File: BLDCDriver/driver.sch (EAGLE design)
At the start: 66 parts, among them Q2 SIZ240DT-T1-GE3, Q3 SIZ240DT-T1-GE3, Q4 SIZ240DT-T1-GE3, U1 QFN50P400X400X100-25NDRV8300D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, U2 AS5048A-HTSP-500, U3 MCP2562-E/SN, U4 SOP80P620X125-8N, X2 JST-XH-06-PIN-LONG-PAD

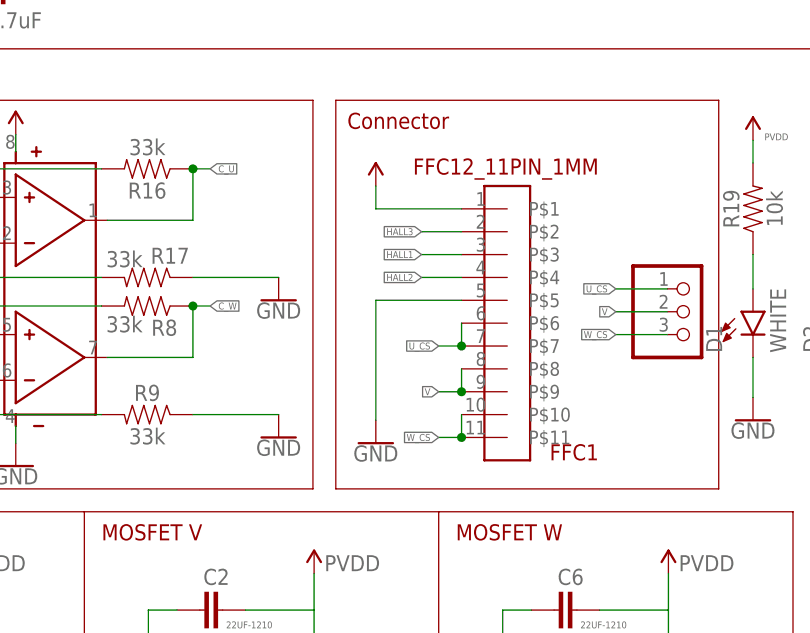
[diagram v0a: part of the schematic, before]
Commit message: ゲートドライバ周りの配線全部終わらせた
# ==== Emojis ====
# ✨ :sparkles: Add new feature
# ✅  :white_check_mark: Update existing feature (not bug)
# ⚠️  :warning: Fix bug/error
# 🔥  :fire: Remove files or features
# ✏️ :pencil2: Fix typos
# 📝  :memo: Update documentation
# ♻️  :recycle: Dependencies update
# 🐧  :penguin: Improved the Linux
# 🍎  :apple: Improved the macOS
# 🔖 :bookmark: Add new library
# 🎉  :tada: Initial commit

# ==== Format ====
# :emoji: Subject
#
# Commit body...

# ==== Messages ====
# 新規(ファイル)機能追加: Add
# 機能修正、既存機能追加（バグではない): Update
# リファクタリング: Clean
# ファイル名変更:
# 削除など: Remove
# バグ修正: Fix
# バージョンアップ: Upgrade
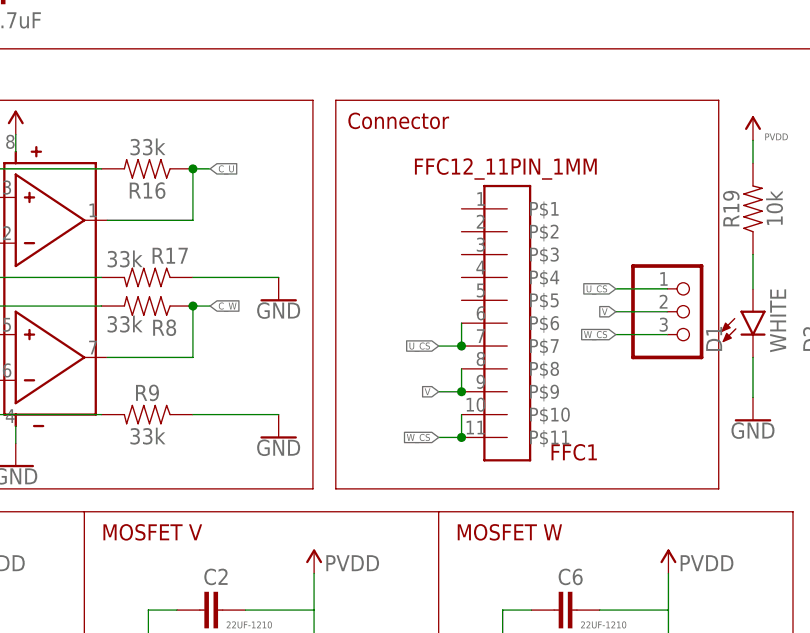
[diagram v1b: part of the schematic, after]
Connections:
- removed net HALL1: FFC1.P$3
- removed net HALL2: FFC1.P$4
- removed net HALL3: FFC1.P$2
- net 5V: no longer FFC1.P$1
- net GND: no longer FFC1.P$5
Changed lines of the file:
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@@
 <part name="GND12" library="SparkFun-PowerSymbols" deviceset="GND" device=""/>
 <part name="FFC1" library="MotorDriver_FourthEdition_prot" deviceset="FFC12_11PIN_1MM" device=""/>
-<part name="SUPPLY8" library="SparkFun-PowerSymbols" deviceset="VCC_1" device="" value="GVDD"/>
-<part name="GND11" library="SparkFun-PowerSymbols" deviceset="GND" device=""/>
 <part name="U2" library="AS5048A-HTSP-500" deviceset="AS5048A-HTSP-500" device=""/>
 <part name="U4" library="NJM2732" deviceset="SOP80P620X125-8N" device=""/>
@@
 <attribute name="VALUE" x="149.225" y="102.87" size="1.778" layer="94" rot="MR0"/>
 </instance>
-<instance part="SUPPLY8" gate="G$2" x="124.46" y="101.6" smashed="yes"/>
-<instance part="GND11" gate="1" x="124.46" y="73.025" smashed="yes">
-<attribute name="VALUE" x="124.46" y="72.771" size="1.778" layer="96" align="top-center"/>
-</instance>
 <instance part="U2" gate="G$1" x="145.415" y="196.85" smashed="yes">
 <attribute name="NAME" x="135.2441" y="212.1063" size="1.27" layer="95"/>
@@
 <wire x1="4.445" y1="34.29" x2="4.445" y2="31.75" width="0.1524" layer="91"/>
 <pinref part="GND12" gate="1" pin="GND"/>
-</segment>
-<segment>
-<pinref part="FFC1" gate="G$1" pin="P$5"/>
-<pinref part="GND11" gate="1" pin="GND"/>
-<wire x1="124.46" y1="75.565" x2="124.46" y2="88.9" width="0.1524" layer="91"/>
-<wire x1="124.46" y1="88.9" x2="133.985" y2="88.9" width="0.1524" layer="91"/>
 </segment>
 <segment>
@@
 </segment>
 </net>
-<net name="HALL3" class="0">
-<segment>
-<pinref part="FFC1" gate="G$1" pin="P$2"/>
-<wire x1="133.985" y1="96.52" x2="129.54" y2="96.52" width="0.1524" layer="91"/>
-<label x="129.54" y="96.52" size="0.762" layer="95" rot="MR0" xref="yes"/>
-</segment>
-</net>
-<net name="HALL1" class="0">
-<segment>
-<pinref part="FFC1" gate="G$1" pin="P$3"/>
-<wire x1="133.985" y1="93.98" x2="129.54" y2="93.98" width="0.1524" layer="91"/>
-<label x="129.54" y="93.98" size="0.762" layer="95" rot="MR0" xref="yes"/>
-</segment>
-</net>
-<net name="HALL2" class="0">
-<segment>
-<pinref part="FFC1" gate="G$1" pin="P$4"/>
-<wire x1="133.985" y1="91.44" x2="129.54" y2="91.44" width="0.1524" layer="91"/>
-<label x="129.54" y="91.44" size="0.762" layer="95" rot="MR0" xref="yes"/>
-</segment>
-</net>
 <net name="5V" class="0">
 <segment>
-<pinref part="SUPPLY8" gate="G$2" pin="VCC_1"/>
-<pinref part="FFC1" gate="G$1" pin="P$1"/>
-<wire x1="133.985" y1="99.06" x2="124.46" y2="99.06" width="0.1524" layer="91"/>
-<wire x1="124.46" y1="101.6" x2="124.46" y2="99.06" width="0.1524" layer="91"/>
-</segment>
-<segment>
 <wire x1="185.42" y1="60.96" x2="182.88" y2="60.96" width="0.1524" layer="91"/>

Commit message: CANの配線をした
# ==== Emojis ====
# ✨ :sparkles: Add new feature
# ✅  :white_check_mark: Update existing feature (not bug)
# ⚠️  :warning: Fix bug/error
# 🔥  :fire: Remove files or features
# ✏️ :pencil2: Fix typos
# 📝  :memo: Update documentation
# ♻️  :recycle: Dependencies update
# 🐧  :penguin: Improved the Linux
# 🍎  :apple: Improved the macOS
# 🔖 :bookmark: Add new library
# 🎉  :tada: Initial commit

# ==== Format ====
# :emoji: Subject
#
# Commit body...

# ==== Messages ====
# 新規(ファイル)機能追加: Add
# 機能修正、既存機能追加（バグではない): Update
# リファクタリング: Clean
# ファイル名変更:
# 削除など: Remove
# バグ修正: Fix
# バージョンアップ: Upgrade
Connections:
- net CANRX: now also NUCLEO_MAIN.PB9
- net CANTX: now also NUCLEO_MAIN.PB8
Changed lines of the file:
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@@
 <label x="180.34" y="22.86" size="0.762" layer="95" rot="R180" xref="yes"/>
+</segment>
+<segment>
+<pinref part="NUCLEO_MAIN" gate="G$1" pin="PB8"/>
+<wire x1="53.34" y1="202.565" x2="53.34" y2="208.28" width="0.1524" layer="91"/>
+<label x="53.34" y="208.28" size="0.762" layer="95" rot="R90" xref="yes"/>
 </segment>
 </net>
@@
 <label x="220.98" y="20.32" size="0.762" layer="95" xref="yes"/>
 </segment>
+<segment>
+<pinref part="NUCLEO_MAIN" gate="G$1" pin="PB9"/>
+<wire x1="50.8" y1="202.565" x2="50.8" y2="208.28" width="0.1524" layer="91"/>
+<label x="50.8" y="208.28" size="0.762" layer="95" rot="R90" xref="yes"/>
+</segment>
 </net>

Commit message: CANトランシーバーの近くにコンデンサつけた
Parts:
- added C23: 0.1uF, SparkFun-Capacitors:0.1UF-0603-100V-10%
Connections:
- net 5V: now also C23.1
- net GND: now also C23.2
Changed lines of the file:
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@@
 <part name="C21" library="SparkFun-Capacitors" deviceset="22UF" device="-1210-16V-20%" value="22UF-1210"/>
 <part name="C22" library="SparkFun-Capacitors" deviceset="22UF" device="-1210-16V-20%" value="22UF-1210"/>
+<part name="C23" library="SparkFun-Capacitors" deviceset="0.1UF" device="-0603-100V-10%" value="0.1uF"/>
 </parts>
 <sheets>
@@
 <attribute name="VALUE" x="142.621" y="14.224" size="0.762" layer="96" font="vector" rot="R180"/>
 </instance>
+<instance part="C23" gate="G$1" x="229.87" y="20.32" smashed="yes">
+<attribute name="NAME" x="231.394" y="23.241" size="1.778" layer="95" font="vector"/>
+<attribute name="VALUE" x="231.394" y="18.161" size="1.778" layer="96" font="vector"/>
+</instance>
 </instances>
 <busses>
@@
 <pinref part="GND10" gate="1" pin="GND"/>
 <label x="220.98" y="15.24" size="0.762" layer="95"/>
+<pinref part="C23" gate="G$1" pin="2"/>
+<wire x1="229.87" y1="17.78" x2="229.87" y2="15.24" width="0.1524" layer="91"/>
+<wire x1="229.87" y1="15.24" x2="220.98" y2="15.24" width="0.1524" layer="91"/>
+<junction x="220.98" y="15.24"/>
 </segment>
 <segment>
@@
 <pinref part="SUPPLY14" gate="G$2" pin="VCC_1"/>
 <label x="219.71" y="27.94" size="0.762" layer="95"/>
-</segment>
-<segment>
+<pinref part="C23" gate="G$1" pin="1"/>
+<wire x1="220.98" y1="25.4" x2="229.87" y2="25.4" width="0.1524" layer="91"/>
+<junction x="220.98" y="25.4"/>
+</segment>
+<segment>

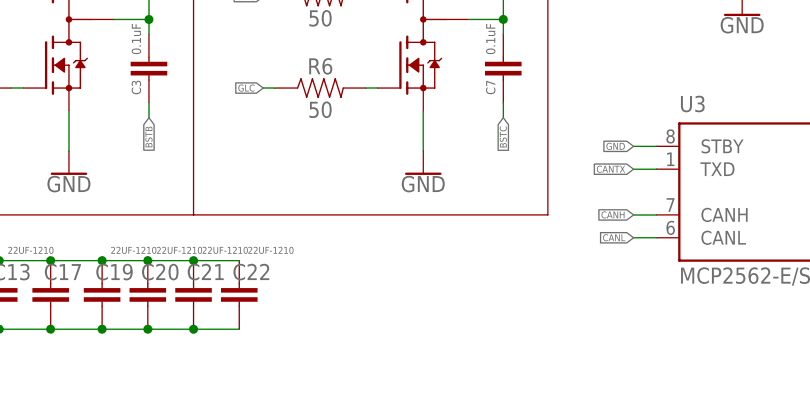
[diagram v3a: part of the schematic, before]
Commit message: ボードをパネライズした
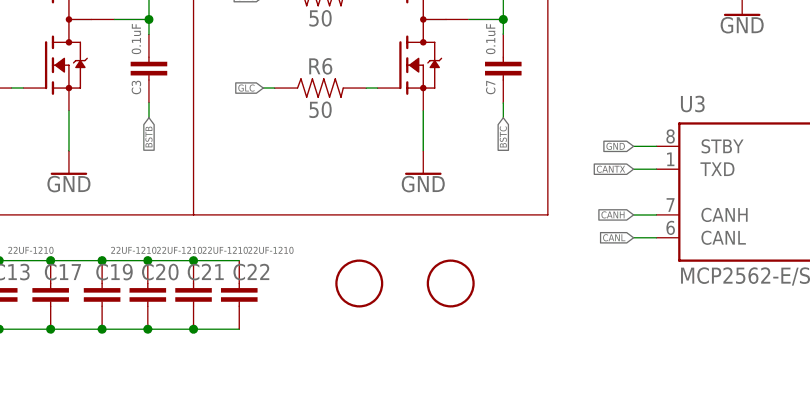
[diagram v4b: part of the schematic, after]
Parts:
- added U$1, U$3: PIN, pin:PIN
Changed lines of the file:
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@@
 <part name="C22" library="SparkFun-Capacitors" deviceset="22UF" device="-1210-16V-20%" value="22UF-1210"/>
 <part name="C23" library="SparkFun-Capacitors" deviceset="0.1UF" device="-0603-100V-10%" value="0.1uF"/>
+<part name="U$1" library="pin" deviceset="PIN" device=""/>
+<part name="U$3" library="pin" deviceset="PIN" device=""/>
 </parts>
 <sheets>
@@
 <attribute name="VALUE" x="231.394" y="18.161" size="1.778" layer="96" font="vector"/>
 </instance>
+<instance part="U$1" gate="G$1" x="149.86" y="10.16" smashed="yes"/>
+<instance part="U$3" gate="G$1" x="160.02" y="10.16" smashed="yes"/>
 </instances>
 <busses>

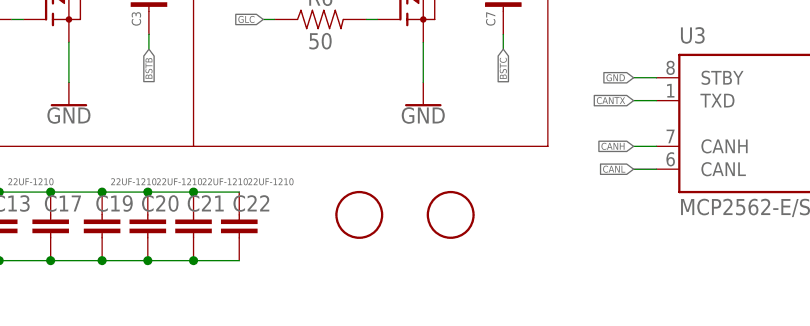
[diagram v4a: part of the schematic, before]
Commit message: 位置合せピンを追加した
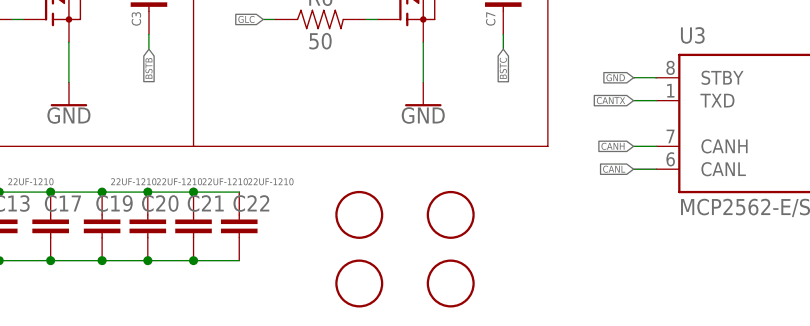
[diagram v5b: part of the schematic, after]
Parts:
- added U$4, U$5: PIN, pin:PIN
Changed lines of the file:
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@@
 <part name="U$1" library="pin" deviceset="PIN" device=""/>
 <part name="U$3" library="pin" deviceset="PIN" device=""/>
+<part name="U$4" library="pin" deviceset="PIN" device=""/>
+<part name="U$5" library="pin" deviceset="PIN" device=""/>
 </parts>
 <sheets>
@@
 <instance part="U$1" gate="G$1" x="149.86" y="10.16" smashed="yes"/>
 <instance part="U$3" gate="G$1" x="160.02" y="10.16" smashed="yes"/>
+<instance part="U$4" gate="G$1" x="149.86" y="2.54" smashed="yes"/>
+<instance part="U$5" gate="G$1" x="160.02" y="2.54" smashed="yes"/>
 </instances>
 <busses>

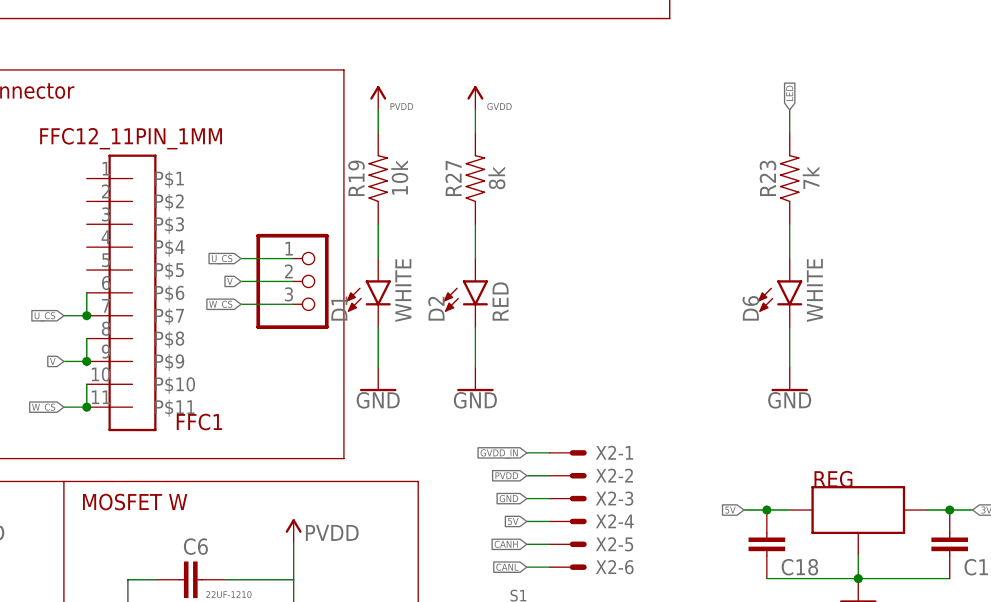
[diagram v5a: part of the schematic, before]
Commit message: 部品の数値を編集
# ==== Emojis ====
# ✨ :sparkles: Add new feature
# ✅  :white_check_mark: Update existing feature (not bug)
# ⚠️  :warning: Fix bug/error
# 🔥  :fire: Remove files or features
# ✏️ :pencil2: Fix typos
# 📝  :memo: Update documentation
# ♻️  :recycle: Dependencies update
# 🐧  :penguin: Improved the Linux
# 🍎  :apple: Improved the macOS
# 🔖 :bookmark: Add new library
# 🎉  :tada: Initial commit

# ==== Format ====
# :emoji: Subject
#
# Commit body...

# ==== Messages ====
# 新規(ファイル)機能追加: Add
# 機能修正、既存機能追加（バグではない): Update
# リファクタリング: Clean
# ファイル名変更:
# 削除など: Remove
# バグ修正: Fix
# バージョンアップ: Upgrade
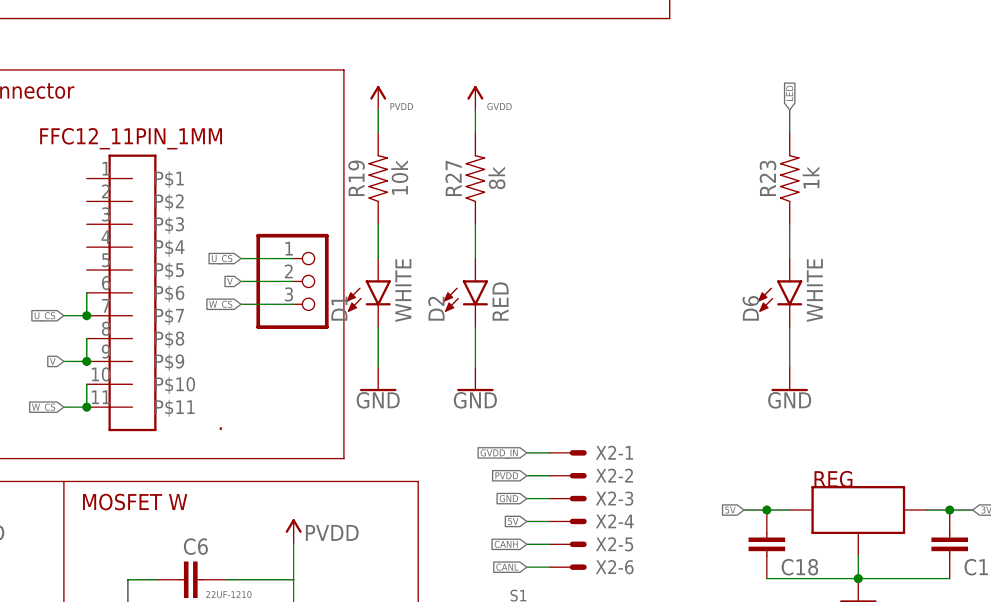
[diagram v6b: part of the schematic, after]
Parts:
- R23: value 7k -> 1k
- renumbered FFC1 to .
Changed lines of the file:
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@@
 <part name="GND6" library="SparkFun-PowerSymbols" deviceset="GND" device=""/>
 <part name="GND12" library="SparkFun-PowerSymbols" deviceset="GND" device=""/>
-<part name="FFC1" library="MotorDriver_FourthEdition_prot" deviceset="FFC12_11PIN_1MM" device=""/>
+<part name="." library="MotorDriver_FourthEdition_prot" deviceset="FFC12_11PIN_1MM" device=""/>
 <part name="U2" library="AS5048A-HTSP-500" deviceset="AS5048A-HTSP-500" device=""/>
 <part name="U4" library="NJM2732" deviceset="SOP80P620X125-8N" device=""/>
@@
 <part name="GND24" library="SparkFun-PowerSymbols" deviceset="GND" device=""/>
 <part name="D6" library="SparkFun-LED" library_urn="urn:adsk.eagle:library:529" deviceset="LED-WHITE" device="0603" package3d_urn="urn:adsk.eagle:package:39354/1" value="WHITE"/>
-<part name="R23" library="SparkFun-Resistors" library_urn="urn:adsk.eagle:library:532" deviceset="2.0KOHM" device="-0603-1/10W-5%" package3d_urn="urn:adsk.eagle:package:39650/1" value="7k"/>
+<part name="R23" library="SparkFun-Resistors" library_urn="urn:adsk.eagle:library:532" deviceset="2.0KOHM" device="-0603-1/10W-5%" package3d_urn="urn:adsk.eagle:package:39650/1" value="1k"/>
 <part name="GND25" library="SparkFun-PowerSymbols" deviceset="GND" device=""/>
 <part name="Q2" library="SIZ240DT-T1-GE3" deviceset="SIZ240DT-T1-GE3" device=""/>
@@
 <attribute name="VALUE" x="4.445" y="28.956" size="1.778" layer="96" align="top-center"/>
 </instance>
-<instance part="FFC1" gate="G$1" x="139.065" y="86.36" smashed="yes" rot="MR0">
+<instance part="." gate="G$1" x="139.065" y="86.36" smashed="yes" rot="MR0">
 <attribute name="NAME" x="149.225" y="71.12" size="1.778" layer="94" rot="MR0"/>
 <attribute name="VALUE" x="149.225" y="102.87" size="1.778" layer="94" rot="MR0"/>
@@
 </segment>
 <segment>
-<pinref part="FFC1" gate="G$1" pin="P$9"/>
-<pinref part="FFC1" gate="G$1" pin="P$8"/>
+<pinref part="." gate="G$1" pin="P$9"/>
+<pinref part="." gate="G$1" pin="P$8"/>
 <wire x1="133.985" y1="78.74" x2="133.985" y2="81.28" width="0.1524" layer="91"/>
 <wire x1="133.985" y1="78.74" x2="131.445" y2="78.74" width="0.1524" layer="91"/>
@@
 <net name="U_CS" class="0">
 <segment>
-<pinref part="FFC1" gate="G$1" pin="P$7"/>
+<pinref part="." gate="G$1" pin="P$7"/>
 <wire x1="133.985" y1="83.82" x2="131.445" y2="83.82" width="0.1524" layer="91"/>
-<pinref part="FFC1" gate="G$1" pin="P$6"/>
+<pinref part="." gate="G$1" pin="P$6"/>
 <wire x1="133.985" y1="83.82" x2="133.985" y2="86.36" width="0.1524" layer="91"/>
 <junction x="133.985" y="83.82"/>
@@
 </segment>
 <segment>
-<pinref part="FFC1" gate="G$1" pin="P$11"/>
-<pinref part="FFC1" gate="G$1" pin="P$10"/>
+<pinref part="." gate="G$1" pin="P$11"/>
+<pinref part="." gate="G$1" pin="P$10"/>
 <wire x1="133.985" y1="73.66" x2="133.985" y2="76.2" width="0.1524" layer="91"/>
 <wire x1="133.985" y1="73.66" x2="131.445" y2="73.66" width="0.1524" layer="91"/>

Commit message: 発注します
# ==== Emojis ====
# ✨ :sparkles: Add new feature
# ✅  :white_check_mark: Update existing feature (not bug)
# ⚠️  :warning: Fix bug/error
# 🔥  :fire: Remove files or features
# ✏️ :pencil2: Fix typos
# 📝  :memo: Update documentation
# ♻️  :recycle: Dependencies update
# 🐧  :penguin: Improved the Linux
# 🍎  :apple: Improved the macOS
# 🔖 :bookmark: Add new library
# 🎉  :tada: Initial commit

# ==== Format ====
# :emoji: Subject
#
# Commit body...

# ==== Messages ====
# 新規(ファイル)機能追加: Add
# 機能修正、既存機能追加（バグではない): Update
# リファクタリング: Clean
# ファイル名変更:
# 削除など: Remove
# バグ修正: Fix
# バージョンアップ: Upgrade
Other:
- note added: "CAN"
- note added: "EXT"
- note added: "LED"
- note added: "SW"
- moved on the sheet: C10, C11, C12, C13, C16, C17, C18, C19, C20, C21, C22, C23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
